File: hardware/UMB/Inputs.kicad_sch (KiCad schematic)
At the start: 30 parts, among them J1 FTSH-107-01-L-D-K, J10 Conn_01x04, J11 Conn_01x04, J12 Conn_01x04, J13 Conn_01x04, J14 Conn_01x04, J15 Conn_01x04, J2 Conn_01x02, J3 Conn_01x02, J4 Conn_01x03, J5 Conn_01x03, J6 Conn_01x03, J7 Conn_01x03, J8 Conn_01x03, J9 Conn_01x03

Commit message: Power section done
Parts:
- removed J10, J11, J12, J13, J14, J15: Conn_01x04, symbol Connector_Generic:Conn_01x04
- added J10, J11, J12, J13, J7, J8: Conn_01x05, symbol Connector_Generic:Conn_01x05
- renumbered D15 to D10, D16 to D11, D26 to D12, D27 to D13, D17 to D14, D18 to D15, D13 to D16, D20 to D17, D19 to D18, D21 to D19, D22 to D20, D23 to D21, D25 to D22, D to D8, D14 to D9, J4 to J14, J5 to J15, J3 to J16, J2 to J17, J6 to J18, J7 to J19, J8 to J20, J9 to J21, J1 to J9
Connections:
- net +5V: now also J10.4 (Pin_4), J11.4 (Pin_4), J12.4 (Pin_4), J13.4 (Pin_4), J7.4 (Pin_4), J8.4 (Pin_4)
- net DIF1+: now also J7.3 (Pin_3)
- net DIF1-: now also J7.2 (Pin_2)
- net DIF2+: now also J10.3 (Pin_3)
- net DIF2-: now also J10.2 (Pin_2)
- net DIF3+: now also J12.3 (Pin_3)
- net DIF3-: now also J12.2 (Pin_2)
- net DIF4+: now also J8.3 (Pin_3)
- net DIF4-: now also J8.2 (Pin_2)
- net DIF5+: now also J11.3 (Pin_3)
- net DIF5-: now also J11.2 (Pin_2)
- net DIF6+: now also J13.3 (Pin_3)
- net DIF6-: now also J13.2 (Pin_2)
- net GND: now also J10.1 (Pin_1), J11.1 (Pin_1), J12.1 (Pin_1), J13.1 (Pin_1), J7.1 (Pin_1), J8.1 (Pin_1)
- net SE1in renamed SE1IN
- net SE1IN: now also D17.1 (A1)
- net SE2in renamed SE2IN
- net SE2IN: now also D19.1 (A1)
- net SE3in renamed SE3IN
- net SE3IN: now also D21.1 (A1)
- removed net SE4in: D17.1 (A1), D18.1 (A1), D19.1 (A1), D20.1 (A1), D21.1 (A1), D22.1 (A1), J15.2 (Pin_2)
- net SE5in renamed SE5IN
- net SE5IN: now also D20.1 (A1)
- net SE6in renamed SE6IN
- net SE6IN: now also D22.1 (A1)
- new net +12V: J10.5 (Pin_5), J11.5 (Pin_5), J12.5 (Pin_5), J13.5 (Pin_5), J7.5 (Pin_5), J8.5 (Pin_5)
- new net SE4IN: D18.1 (A1), J15.2 (Pin_2)
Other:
- note added: "SWO not connected bc MCU doesn`t support it"
- note removed: "SWO not connected bc no pin for it on MCU"
- moved on the sheet: D10, D11, D12, D13, D14, D15, D16, D17, D18, D19, D20, D21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

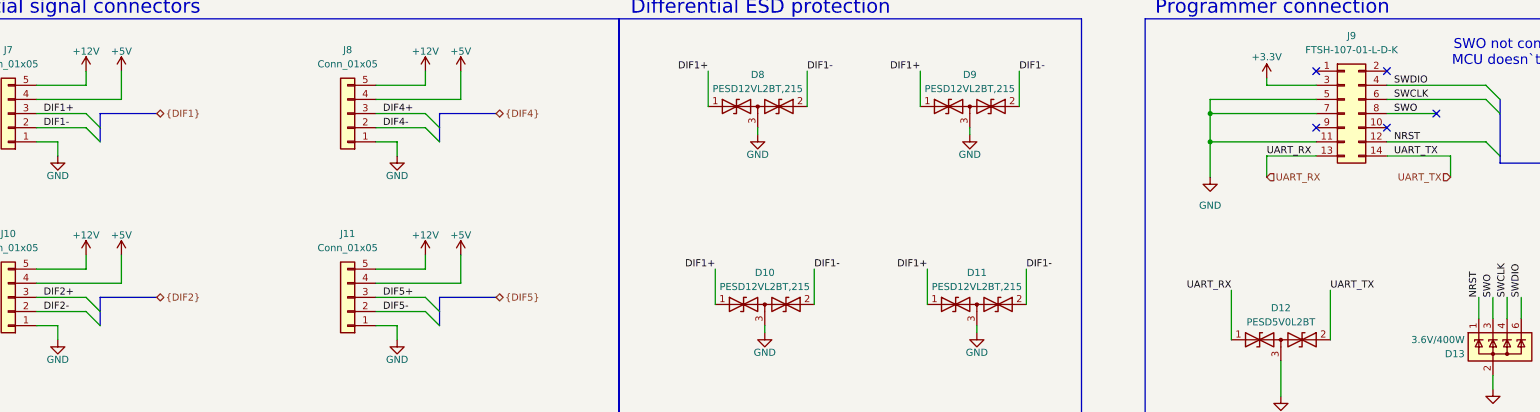
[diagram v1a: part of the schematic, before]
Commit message: Added all footprints and parts Mouser IDs
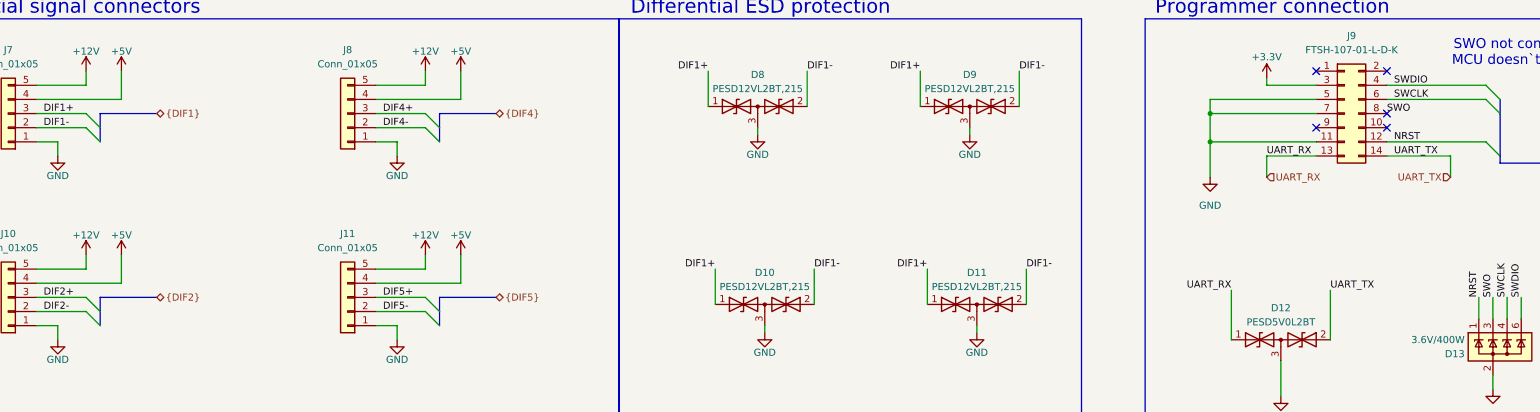
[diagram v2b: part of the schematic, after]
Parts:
- D10, D11, D14, D15, D8, D9: Manufacturer_Part_Number (none) -> D5V0L2B3W-7; Mouser (none) -> https://www.mouser.pl/ProductDetail/Diodes-Incorporated/D5V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; Mouser No (none) -> 621-D5V0L2B3W-7; Mouser Part Number 771-PESD12VL2BT-T/R -> (none)
- D12, D16: Manufacturer_Part_Number (none) -> PESD5V0L2BT-QR; Mouser (none) -> https://www.mouser.pl/ProductDetail/Nexperia/PESD5V0L2BT-QR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; Mouser No (none) -> 771-PESD5V0L2BT-QR; Mouser Part Number 771-PESD5V0L2BT-QR -> (none)
- D13: Mouser (none) -> https://www.mouser.pl/ProductDetail/Texas-Instruments/ESDS3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; Mouser No (none) -> 595-ESDS304DBVR; Mouser Part Number 595-ESDS304DBVR -> (none)
- D17, D18, D19, D20, D21, D22: Manufacturer_Part_Number (none) -> SZESD9101P2T5G; Mouser (none) -> https://www.mouser.pl/ProductDetail/onsemi/SZESD9101P2T5G?q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; Mouser No (none) -> 863-SZESD9101P2T5G; Mouser link https://www.mouser.pl/ProductDetail/onsemi/SZESD9101P2T5G?q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 -> (none)
- J10, J11, J12, J13, J7, J8: footprint (none) -> Wago_01x05:26011105
- J14, J15, J18, J19, J20, J21: footprint (none) -> Wago_01x03:26011103
- J16, J17: footprint (none) -> Wago_01x02:26011102
- J9: Manufacturer_Name SAMTEC -> (none); Mouser (none) -> https://www.mouser.pl/ProductDetail/Samtec/FTSH-107-01-L-D-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; Mouser No (none) -> 200-FTSH10701LDK; Mouser Part Number 200-FTSH10701LDK -> (none); Mouser Price/Stock https://www.mouser.co.uk/ProductDetail/Samtec/FTSH-107-01-L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 -> (none)
